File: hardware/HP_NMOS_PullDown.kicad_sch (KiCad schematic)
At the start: 3 parts, among them Q6 Q_NMOS_GDS

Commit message: schemat sync
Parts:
- added D13: D_Small, symbol Device:D_Small
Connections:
- net OUT is gone; now on net GND: Q6.3 (S)
- net IN: now also D13.2 (A)
- new net SAFETY_AIR: D13.1 (K)
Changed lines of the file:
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@@
 (kicad_sch (version 20211123) (generator eeschema)
   (paper "A4")
+  (junction (at 135.255 94.615) (diameter 0) (color 0 0 0 0)
+  )
+  (junction (at 144.145 73.025) (diameter 0) (color 0 0 0 0)
+  )
   (junction (at 135.255 86.995) (diameter 0) (color 0 0 0 0)
+  )
+  (junction (at 144.145 80.645) (diameter 0) (color 0 0 0 0)
   )
   (wire (pts (xy 132.715 86.995) (xy 135.255 86.995))
     (stroke (width 0) (type default) (color 0 0 0 0))
   )
-  (wire (pts (xy 144.145 80.645) (xy 145.415 80.645))
+  (wire (pts (xy 144.145 80.645) (xy 146.685 80.645))
     (stroke (width 0) (type default) (color 0 0 0 0))
   )
@@
     (stroke (width 0) (type default) (color 0 0 0 0))
   )
-  (wire (pts (xy 144.145 93.345) (xy 145.415 93.345))
+  (wire (pts (xy 135.255 86.995) (xy 136.525 86.995))
     (stroke (width 0) (type default) (color 0 0 0 0))
   )
-  (wire (pts (xy 135.255 86.995) (xy 136.525 86.995))
+  (wire (pts (xy 135.255 94.615) (xy 135.255 95.885))
     (stroke (width 0) (type default) (color 0 0 0 0))
   )
@@
     (stroke (width 0) (type default) (color 0 0 0 0))
   )
-  (wire (pts (xy 144.145 92.075) (xy 144.145 93.345))
+  (wire (pts (xy 144.145 73.025) (xy 144.145 74.295))
     (stroke (width 0) (type default) (color 0 0 0 0))
   )
@@
     (stroke (width 0) (type default) (color 0 0 0 0))
   )
+  (wire (pts (xy 144.145 92.075) (xy 144.145 94.615))
+    (stroke (width 0) (type default) (color 0 0 0 0))
+  )
+  (wire (pts (xy 144.145 73.025) (xy 141.605 73.025))
+    (stroke (width 0) (type default) (color 0 0 0 0))
+  )
+  (wire (pts (xy 144.145 79.375) (xy 144.145 80.645))
+    (stroke (width 0) (type default) (color 0 0 0 0))
+  )
+  (wire (pts (xy 135.255 94.615) (xy 144.145 94.615))
+    (stroke (width 0) (type default) (color 0 0 0 0))
+  )
   (wire (pts (xy 144.145 81.915) (xy 144.145 80.645))
     (stroke (width 0) (type default) (color 0 0 0 0))
   )
-  (hierarchical_label "IN" (shape input) (at 145.415 80.645 0)
+  (wire (pts (xy 146.685 73.025) (xy 144.145 73.025))
+    (stroke (width 0) (type default) (color 0 0 0 0))
+  )
+  (global_label "SAFETY_AIR" (shape input) (at 141.605 73.025 180) (fields_autoplaced)
+    (effects (font (size 1.27 1.27)) (justify right))
+    (property "Intersheet References" "${INTERSHEET_REFS}" (id 0) (at 128.7579 73.1044 0)
+      (effects (font (size 1.27 1.27)) (justify right) hide)
+    )
+  )
+  (hierarchical_label "IN" (shape input) (at 146.685 80.645 0)
     (effects (font (size 1.27 1.27)) (justify left))
   )
-  (hierarchical_label "OUT" (shape output) (at 145.415 93.345 0)
+  (hierarchical_label "OUT" (shape output) (at 146.685 73.025 0)
     (effects (font (size 1.27 1.27)) (justify left))
   )
@@
     (pin "3")
   )
-  (symbol (lib_id "power:GND") (at 135.255 94.615 0)
-    (in_bom yes) (on_board yes)
-    (property "Reference" "#PWR0127" (id 0) (at 135.255 100.965 0)
+  (symbol (lib_id "Device:D_Small") (at 144.145 76.835 270)
+    (in_bom yes) (on_board yes) (fields_autoplaced)
+    (property "Reference" "D13" (id 0) (at 146.05 75.5649 90)
+      (effects (font (size 1.27 1.27)) (justify left))
+    )
+    (property "Value" "D_Small" (id 1) (at 146.05 78.1049 90)
+      (effects (font (size 1.27 1.27)) (justify left))
+    )
+    (property "Footprint" "" (id 2) (at 144.145 76.835 90)
       (effects (font (size 1.27 1.27)) hide)
     )
-    (property "Value" "GND" (id 1) (at 135.382 99.0092 0))
-    (property "Footprint" "" (id 2) (at 135.255 94.615 0)
+    (property "Datasheet" "~" (id 3) (at 144.145 76.835 90)
       (effects (font (size 1.27 1.27)) hide)
     )
-    (property "Datasheet" "" (id 3) (at 135.255 94.615 0)
+    (pin "1")
+    (pin "2")
+  )
+  (symbol (lib_id "power:GND") (at 135.255 95.885 0)
+    (in_bom yes) (on_board yes)
+    (property "Reference" "#PWR0127" (id 0) (at 135.255 102.235 0)
       (effects (font (size 1.27 1.27)) hide)
     )
+    (property "Value" "GND" (id 1) (at 135.382 100.2792 0))
+    (property "Footprint" "" (id 2) (at 135.255 95.885 0)
+      (effects (font (size 1.27 1.27)) hide)
+    )
+    (property "Datasheet" "" (id 3) (at 135.255 95.885 0)
+      (effects (font (size 1.27 1.27)) hide)
+    )

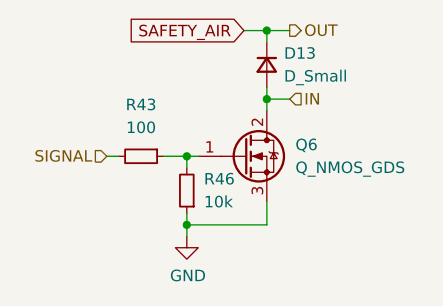
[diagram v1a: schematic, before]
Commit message: measurments section changes, sorted components on the board into groups, changed main connector and added seprate for AIRs, added IMD PWM input as well as AIR fault detection
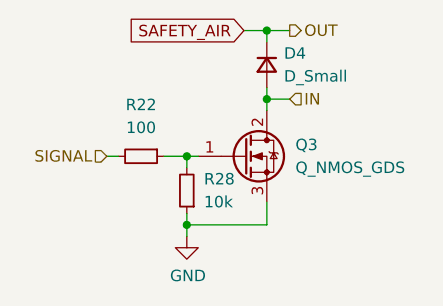
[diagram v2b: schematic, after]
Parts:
- D4: renamed from D13; footprint (none) -> Diode_SMD:D_SMB
- renumbered Q6 to Q3, R43 to R22, R46 to R28
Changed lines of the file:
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@@
   (symbol (lib_id "Device:R_Small") (at 135.255 90.805 180)
     (in_bom yes) (on_board yes) (fields_autoplaced)
-    (property "Reference" "R46" (id 0) (at 137.16 89.5349 0)
+    (property "Reference" "R28" (id 0) (at 137.16 89.5349 0)
       (effects (font (size 1.27 1.27)) (justify right))
     )
@@
   (symbol (lib_id "Device:R_Small") (at 130.175 86.995 270)
     (in_bom yes) (on_board yes) (fields_autoplaced)
-    (property "Reference" "R43" (id 0) (at 130.175 81.28 90))
+    (property "Reference" "R22" (id 0) (at 130.175 81.28 90))
     (property "Value" "100" (id 1) (at 130.175 83.82 90))
     (property "Footprint" "Resistor_SMD:R_0603_1608Metric" (id 2) (at 130.175 86.995 0)
@@
   (symbol (lib_id "Device:Q_NMOS_GDS") (at 141.605 86.995 0)
     (in_bom yes) (on_board yes) (fields_autoplaced)
-    (property "Reference" "Q6" (id 0) (at 147.32 85.7249 0)
+    (property "Reference" "Q3" (id 0) (at 147.32 85.7249 0)
       (effects (font (size 1.27 1.27)) (justify left))
     )
@@
   (symbol (lib_id "Device:D_Small") (at 144.145 76.835 270)
     (in_bom yes) (on_board yes) (fields_autoplaced)
-    (property "Reference" "D13" (id 0) (at 146.05 75.5649 90)
+    (property "Reference" "D4" (id 0) (at 146.05 75.5649 90)
       (effects (font (size 1.27 1.27)) (justify left))
     )
@@
       (effects (font (size 1.27 1.27)) (justify left))
     )
-    (property "Footprint" "" (id 2) (at 144.145 76.835 90)
+    (property "Footprint" "Diode_SMD:D_SMB" (id 2) (at 144.145 76.835 90)
       (effects (font (size 1.27 1.27)) hide)
     )

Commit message: hv elem positioning update'
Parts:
- renumbered D4 to D13, Q3 to Q6, R22 to R43, R28 to R46
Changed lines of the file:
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@@
   (symbol (lib_id "Device:R_Small") (at 135.255 90.805 180)
     (in_bom yes) (on_board yes) (fields_autoplaced)
-    (property "Reference" "R28" (id 0) (at 137.16 89.5349 0)
+    (property "Reference" "R46" (id 0) (at 137.16 89.5349 0)
       (effects (font (size 1.27 1.27)) (justify right))
     )
@@
   (symbol (lib_id "Device:R_Small") (at 130.175 86.995 270)
     (in_bom yes) (on_board yes) (fields_autoplaced)
-    (property "Reference" "R22" (id 0) (at 130.175 81.28 90))
+    (property "Reference" "R43" (id 0) (at 130.175 81.28 90))
     (property "Value" "100" (id 1) (at 130.175 83.82 90))
     (property "Footprint" "Resistor_SMD:R_0603_1608Metric" (id 2) (at 130.175 86.995 0)
@@
   (symbol (lib_id "Device:Q_NMOS_GDS") (at 141.605 86.995 0)
     (in_bom yes) (on_board yes) (fields_autoplaced)
-    (property "Reference" "Q3" (id 0) (at 147.32 85.7249 0)
+    (property "Reference" "Q6" (id 0) (at 147.32 85.7249 0)
       (effects (font (size 1.27 1.27)) (justify left))
     )
@@
   (symbol (lib_id "Device:D_Small") (at 144.145 76.835 270)
     (in_bom yes) (on_board yes) (fields_autoplaced)
-    (property "Reference" "D4" (id 0) (at 146.05 75.5649 90)
+    (property "Reference" "D13" (id 0) (at 146.05 75.5649 90)
       (effects (font (size 1.27 1.27)) (justify left))
     )

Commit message: remake in progress
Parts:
- renumbered D13 to D12, Q6 to Q5, R43 to R30, R46 to R39

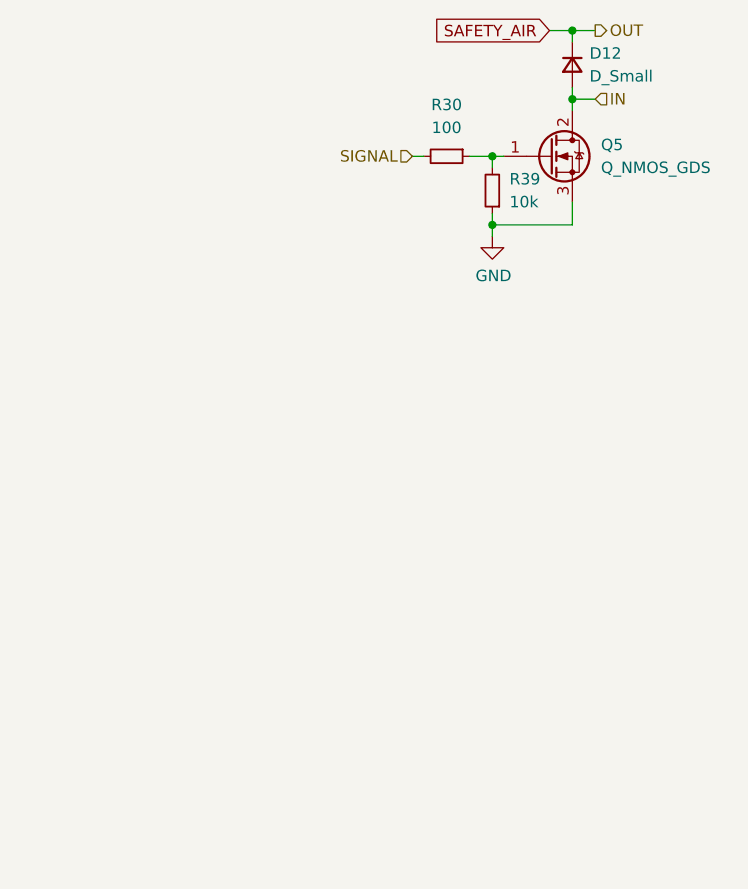
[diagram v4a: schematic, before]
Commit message: major changes: conn, fans, inputs and others
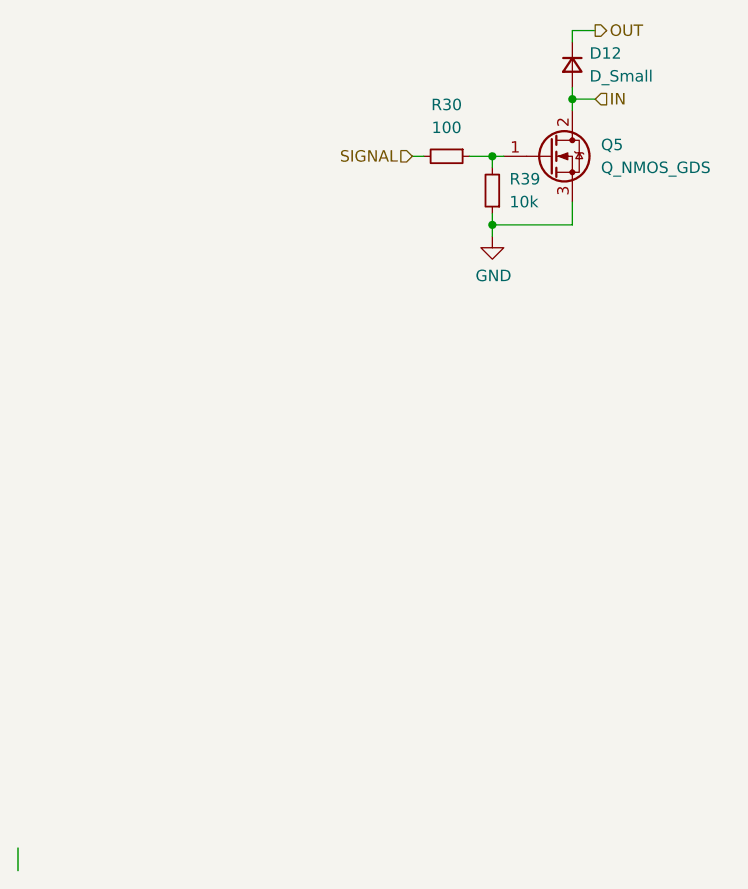
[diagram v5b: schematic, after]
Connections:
- net SAFETY_AIR renamed OUT
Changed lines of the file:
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@@
   (junction (at 135.255 94.615) (diameter 0) (color 0 0 0 0)
-  )
-  (junction (at 144.145 73.025) (diameter 0) (color 0 0 0 0)
   )
   (junction (at 135.255 86.995) (diameter 0) (color 0 0 0 0)
   )
   (junction (at 144.145 80.645) (diameter 0) (color 0 0 0 0)
+  )
+  (wire (pts (xy 82.55 163.83) (xy 82.55 166.37))
+    (stroke (width 0) (type default))
   )
   (wire (pts (xy 132.715 86.995) (xy 135.255 86.995))
@@
     (stroke (width 0) (type default))
   )
-  (wire (pts (xy 144.145 73.025) (xy 141.605 73.025))
-    (stroke (width 0) (type default))
-  )
   (wire (pts (xy 144.145 79.375) (xy 144.145 80.645))
     (stroke (width 0) (type default))
@@
     (stroke (width 0) (type default))
   )
-  (global_label "SAFETY_AIR" (shape input) (at 141.605 73.025 180) (fields_autoplaced)
-    (effects (font (size 1.27 1.27)) (justify right))
-    (property "Intersheetrefs" "${INTERSHEET_REFS}" (at 128.7579 73.1044 0)
-      (effects (font (size 1.27 1.27)) (justify right) hide)
-    )
-  )
   (hierarchical_label "IN" (shape input) (at 146.685 80.645 0) (fields_autoplaced)

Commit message: further improvements
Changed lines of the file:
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@@
   (junction (at 144.145 80.645) (diameter 0) (color 0 0 0 0)
-  )
-  (wire (pts (xy 82.55 163.83) (xy 82.55 166.37))
-    (stroke (width 0) (type default))
   )
   (wire (pts (xy 132.715 86.995) (xy 135.255 86.995))
